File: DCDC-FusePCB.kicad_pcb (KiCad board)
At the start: 2 copper layers, 59 x 39 mm, 11 parts, among them J1 Conn_01x02_Socket, J2 Conn_01x02_Socket

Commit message: precharge board
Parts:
- added C1: 4.7uF, Capacitor_SMD:C_0805_2012Metric, F.Cu at (164.8, 95.3)
- added D1: LED, LED_SMD:LED_0805_2012Metric, F.Cu at (140.1, 102.6)
- added D2: LED, LED_SMD:LED_0805_2012Metric, F.Cu at (150.0, 102.7)
- added J3: Conn_01x02_Socket, Connector_Molex:Molex_Sabre_43160-0102_1x02_P7.49mm_Vertical, F.Cu at (183.5, 94.1)
- added J4: Conn_01x02_Socket, Connector_Molex:Molex_Sabre_43160-0102_1x02_P7.49mm_Vertical, F.Cu at (183.5, 76.2)
- added J5: Precharge Resistor Breakout, Connector_Molex:Molex_Sabre_43160-0102_1x02_P7.49mm_Vertical, F.Cu at (132.1, 86.5)
- added J6: Conn_01x02_Socket, Connector_Molex:Molex_Sabre_43160-0102_1x02_P7.49mm_Vertical, F.Cu at (156.1, 94.1)
- added R1: 10k, Resistor_SMD:R_0805_2012Metric, F.Cu at (144.3, 68.5)
- added R2: 10k, Resistor_SMD:R_0805_2012Metric, F.Cu at (144.2, 79.3)
- added R3: 100k, Resistor_SMD:R_0805_2012Metric, F.Cu at (164.8, 91.4)
- added R4: 22.1k, Resistor_SMD:R_0805_2012Metric, F.Cu at (134.5, 102.6)
- added R5: 22.1k, Resistor_SMD:R_0805_2012Metric, F.Cu at (155.6, 102.7)
- added U1: FDP3651U, footprints:TO-220-3_16P51X10P67_ONS, F.Cu at (131.0, 75.2)
- added U2: TCMT1100, Package_SO:SOP-4_4.4x2.6mm_P1.27mm, F.Cu at (144.3, 73.9)
- added U3: FDP3651U, footprints:TO-220-3_16P51X10P67_ONS, F.Cu at (151.8, 75.1)
- moved J1 62.5 mm to (92.8, 98.8), turned to 0 degrees
- moved G*** 49.6 mm to (164.6, 78.5)
- moved J2 39.1 mm to (92.6, 78.0), turned to 0 degrees
- moved REF** 24.8 mm to (143.3, 95.8)
- moved G*** 23.4 mm to (133.1, 100.6)
- moved G*** 15.7 mm to (153.7, 96.6)
- moved F1 7.49 mm to (120.1, 74.6), turned to -90 degrees
- moved REF** 1.00 mm to (164.0, 70.5)
- moved REF** 1.00 mm to (112.0, 102.5)
- moved REF** 1.00 mm to (112.0, 70.5)
- moved REF** 1.00 mm to (164.0, 102.5)
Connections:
- net Net-(J1-Pin_1) renamed GNDin
- net Net-(J1-Pin_2) renamed HVin
- F1 pad 1: Net-(J2-Pin_2) -> Net-(J5-Pin_1)
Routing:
- net GNDout: track 0.00 -> 69.8 mm, vias 0 -> 2
- net Net-(J2-Pin_2): track 0.00 -> 61.8 mm
- net DC/DC out: track 0.00 -> 58.9 mm
- net Gate_Drive: track 0.00 -> 54.8 mm
- net LowPassIn: track 0.00 -> 41.3 mm
- net LowPassOut: track 0.00 -> 35.9 mm, vias 0 -> 2
- net GNDsupp: track 0.00 -> 33.4 mm
- net +12Vsupp: track 0.00 -> 13.7 mm
- net Net-(J5-Pin_1): track 0.00 -> 12.0 mm
- net Net-(D2-A): track 0.00 -> 3.75 mm
- net Net-(D1-A): track 0.00 -> 3.75 mm
- net Net-(R1-Pad2): track 0.00 -> 2.35 mm
- added copper zone on F.Cu, net GNDout
- added copper zone on F.Cu, net Net-(J5-Pin_1)
- removed copper zone on F.Cu, net Net-(J2-Pin_2)
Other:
- board size 59 x 39 mm -> 112.5 x 39 mm
- board text added: "DC/DC out"
- board text added: "Kadhir was here too"
- board text added: "Precharge Complete"
- board text added: "Precharge Connector"
- board text added: "Supplemental Power"

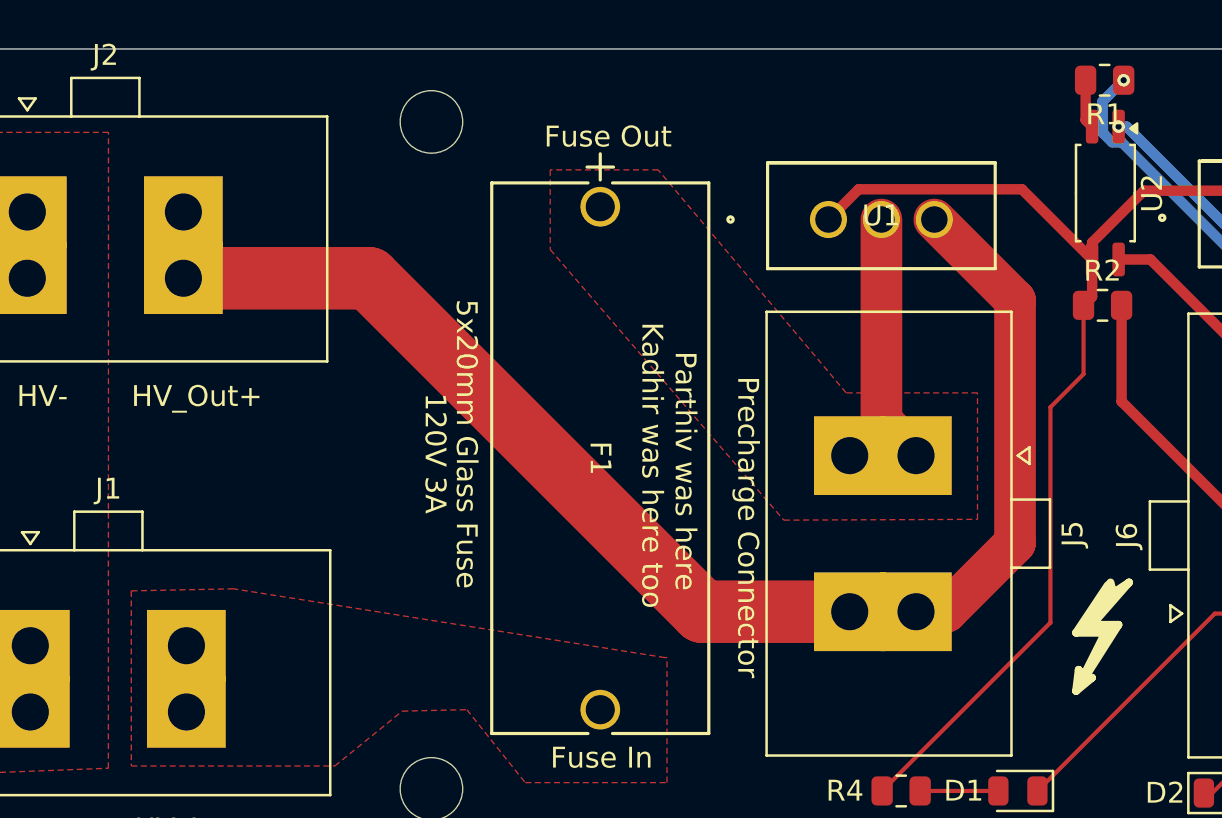
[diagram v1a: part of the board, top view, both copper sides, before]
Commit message: filled zones
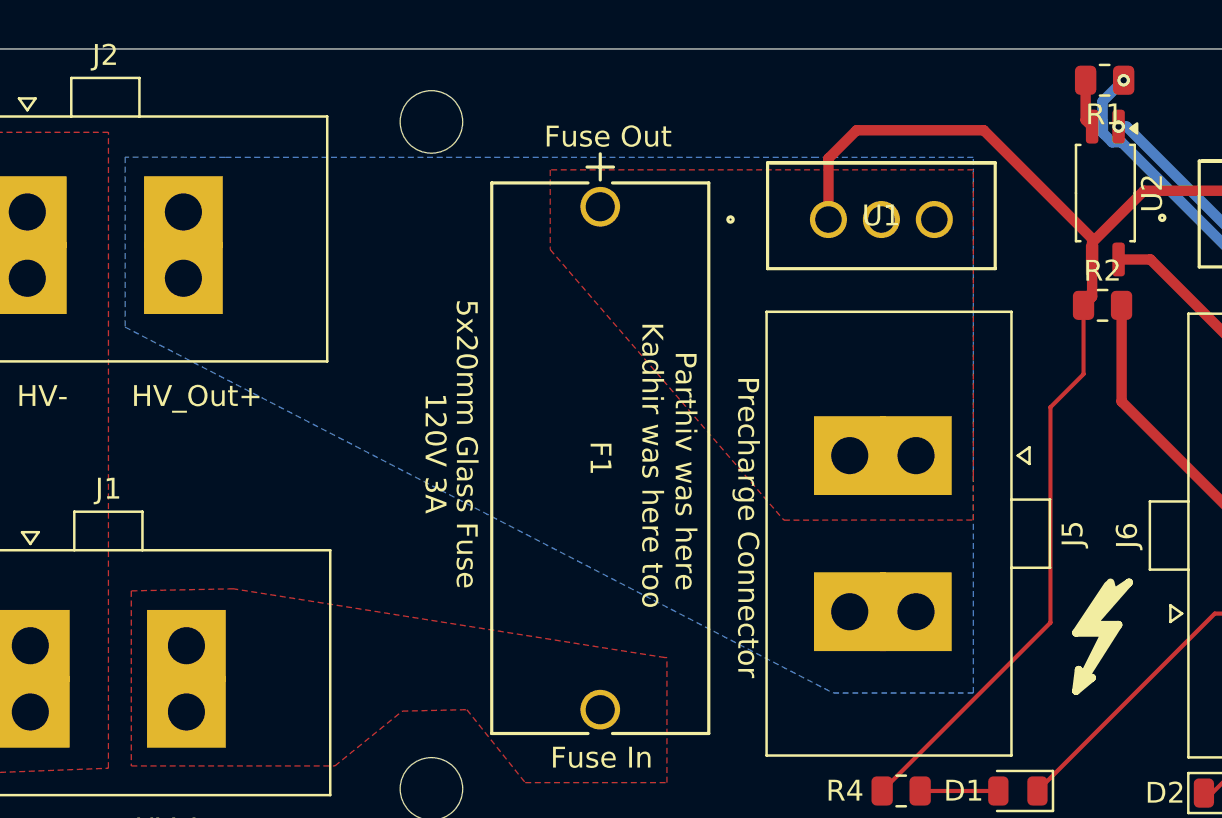
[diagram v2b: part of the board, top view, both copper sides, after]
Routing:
- net Net-(J2-Pin_2): track 61.8 -> 0.00 mm
- net Net-(J5-Pin_1): track 12.0 -> 0.00 mm
- net Gate_Drive: track 54.8 -> 59.4 mm
- added copper zone on B.Cu, net Net-(J2-Pin_2)
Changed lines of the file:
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@@
 			(pinfunction "Pin_1")
 			(pintype "passive")
+			(zone_connect 2)
 		)
 		(pad "1" thru_hole rect
@@
 			(pinfunction "Pin_1")
 			(pintype "passive")
+			(zone_connect 2)
 		)
 		(pad "2" thru_hole rect
@@
 			(pinfunction "Pin_2")
 			(pintype "passive")
+			(zone_connect 2)
 		)
 		(pad "2" thru_hole rect
@@
 			(pinfunction "Pin_2")
 			(pintype "passive")
+			(zone_connect 2)
 		)
 		(embedded_fonts no)
@@
 			(net 2 "Net-(J5-Pin_1)")
 			(pintype "passive")
+			(zone_connect 2)
 		)
 		(pad "2" thru_hole circle
@@
 			(net 11 "HVin")
 			(pintype "passive")
+			(zone_connect 2)
 		)
 		(embedded_fonts no)
@@
 			(pinfunction "Pin_1")
 			(pintype "passive")
+			(zone_connect 2)
 		)
 		(pad "1" thru_hole rect
@@
 			(pinfunction "Pin_1")
 			(pintype "passive")
+			(zone_connect 2)
 		)
 		(pad "2" thru_hole rect
@@
 			(pinfunction "Pin_2")
 			(pintype "passive")
+			(zone_connect 2)
 		)
 		(pad "2" thru_hole rect
@@
 			(pinfunction "Pin_2")
 			(pintype "passive")
+			(zone_connect 2)
 		)
 		(embedded_fonts no)
@@
 			(pinfunction "Pin_1")
 			(pintype "passive")
+			(zone_connect 2)
 		)
 		(pad "1" thru_hole rect
@@
 			(pinfunction "Pin_1")
 			(pintype "passive")
+			(zone_connect 2)
 		)
 		(pad "2" thru_hole rect
@@
 			(pinfunction "Pin_2")
 			(pintype "passive")
+			(zone_connect 2)
 		)
 		(pad "2" thru_hole rect
@@
 			(pinfunction "Pin_2")
 			(pintype "passive")
+			(zone_connect 2)
 		)
 		(embedded_fonts no)
@@
 			(pinfunction "D")
 			(pintype "unspecified")
+			(zone_connect 2)
 		)
 		(pad "3" thru_hole circle
@@
 			(pinfunction "S")
 			(pintype "unspecified")
+			(zone_connect 2)
 		)
 		(embedded_fonts no)
@@
 	)
 	(segment
-		(start 136.129 75.1825)
-		(end 140 79.0535)
-		(width 2)
-		(layer "F.Cu")
-		(net 1)
-	)
-	(segment
-		(start 125 94)
-		(end 132.07 94)
-		(width 3)
-		(layer "F.Cu")
-		(net 1)
-	)
-	(segment
-		(start 140 90.7)
-		(end 136.7 94)
-		(width 2)
-		(layer "F.Cu")
-		(net 1)
-	)
-	(segment
-		(start 140 79.0535)
-		(end 140 90.7)
-		(width 2)
-		(layer "F.Cu")
-		(net 1)
-	)
-	(segment
-		(start 100.1 78)
-		(end 109 78)
-		(width 3)
-		(layer "F.Cu")
-		(net 1)
-	)
-	(segment
-		(start 136.7 94)
-		(end 135.25 94)
-		(width 2)
-		(layer "F.Cu")
-		(net 1)
-	)
-	(segment
-		(start 109 78)
-		(end 125 94)
-		(width 3)
-		(layer "F.Cu")
-		(net 1)
-	)
-	(segment
-		(start 133.589 84.849)
-		(end 135.25 86.51)
-		(width 2)
-		(layer "F.Cu")
-		(net 2)
-	)
-	(segment
-		(start 133.589 75.1825)
-		(end 133.589 84.849)
-		(width 2)
-		(layer "F.Cu")
-		(net 2)
-	)
-	(segment
 		(start 168.95 100.4)
 		(end 180.445 100.4)
@@
 	)
 	(segment
+		(start 143.7 77.1)
+		(end 143.7 76.1)
+		(width 0.5)
+		(layer "F.Cu")
+		(net 9)
+	)
+	(segment
 		(start 146.187501 73.8)
 		(end 150.46 73.8)
@@
 	)
 	(segment
-		(start 140.3315 73.7315)
-		(end 132.5 73.7315)
+		(start 132.4 70.9)
+		(end 131.049 72.251)
 		(width 0.5)
 		(layer "F.Cu")
@@
 	)
 	(segment
-		(start 141.7 84.1875)
-		(end 143.2875 82.6)
-		(width 0.2)
+		(start 131.049 72.251)
+		(end 131.049 75.1825)
+		(width 0.5)
 		(layer "F.Cu")
 		(net 9)
 	)
 	(segment
-		(start 143.7 78.8875)
-		(end 143.2875 79.3)
+		(start 143.7 76.1)
+		(end 138.5 70.9)
 		(width 0.5)
 		(layer "F.Cu")
@@
 	)
 	(segment
-		(start 132.5 73.7315)
-		(end 131.049 75.1825)
+		(start 141.7 84.1875)
+		(end 143.2875 82.6)
+		(width 0.2)
+		(layer "F.Cu")
+		(net 9)
+	)
+	(segment
+		(start 143.7 78.8875)
+		(end 143.2875 79.3)
 		(width 0.5)
 		(layer "F.Cu")
@@
 	)
 	(segment
-		(start 143.7 77.1)
-		(end 140.3315 73.7315)
+		(start 138.5 70.9)
+		(end 132.4 70.9)
 		(width 0.5)
 		(layer "F.Cu")
@@
 		(polygon
 			(pts
-				(xy 117.7 72.8) (xy 117.7 76.626327) (xy 128.909448 89.605688) (xy 138.2 89.567681) (xy 138.2 83.5)
-				(xy 131.9 83.5) (xy 122.877774 72.8)
+				(xy 117.7 72.8) (xy 117.7 76.626327) (xy 128.909448 89.605688) (xy 138 89.6) (xy 138 87.469193)
+				(xy 138 72.8) (xy 123.1 72.8)
 			)
 		)
@@
 			)
 		)
+	)
+	(zone
+		(net 1)
+		(net_name "Net-(J2-Pin_2)")
+		(layer "B.Cu")
+		(hatch edge 0.5)
+		(priority 4)
+		(connect_pads
+			(clearance 0.5)
+		)
+		(min_thickness 0.25)
+		(filled_areas_thickness no)
+		(fill yes
+			(thermal_gap 0.5)
+			(thermal_bridge_width 0.5)
+		)
+		(polygon
+			(pts
+				(xy 97.3 72.187271) (xy 97.3 80.343126) (xy 131.270994 97.9) (xy 138 97.9) (xy 138 72.2) (xy 132.9 72.2)
+				(xy 130.5 72.2) (xy 102.1 72.2)
+			)
+		)

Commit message: Changes
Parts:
- removed U1, U3: FDP3651U, footprints:TO-220-3_16P51X10P67_ONS
- added Q1: IPI200N15N3_G, footprints:TO-220-3_16P51X10P67_ONS, F.Cu at (177.0, 79.0)
- added Q2: IPI200N15N3_G, footprints:TO-220-3_16P51X10P67_ONS, F.Cu at (197.8, 79.0)
- added REF**: MountingHole_3mm, MountingHole:MountingHole_3mm, F.Cu at (70.9, 74.3)
- added REF**: MountingHole_3mm, MountingHole:MountingHole_3mm, F.Cu at (70.9, 106.3)
- added RH1: MountingHole, MountingHole:MountingHole_3.2mm_M3, F.Cu at (120.3, 80.0)
- added RH2: MountingHole, MountingHole:MountingHole_3.2mm_M3, F.Cu at (80.6, 101.5)
- moved D1 46.1 mm to (186.1, 106.4)
- moved D2 46.1 mm to (196.0, 106.5)
- moved F1 46.1 mm to (166.1, 78.4)
- moved G*** 46.1 mm to (210.6, 82.3)
- moved G*** 46.1 mm to (199.7, 100.4)
- moved G*** 46.1 mm to (179.1, 104.4)
- moved J1 46.1 mm to (138.7, 102.6)
- moved J3 46.1 mm to (229.5, 97.9)
- moved J4 46.1 mm to (229.5, 80.0)
- moved J5 46.1 mm to (178.1, 90.3)
- moved R2 46.1 mm to (190.2, 83.1)
- moved R4 46.1 mm to (180.5, 106.4)
- moved R5 46.1 mm to (201.6, 106.5)
- moved REF** 46.1 mm to (210.0, 74.3)
- moved REF** 46.1 mm to (158.0, 106.3)
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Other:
- board size 112.5 x 39 mm -> 172.9 x 39 mm
- board text added: "DCDC Precharge UTSVT Summer 2025"
- board text added: "Precharge Resistor"
